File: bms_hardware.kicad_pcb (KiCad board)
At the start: 2 copper layers, 150.6 x 71.7 mm, 199 parts, among them J1 Conn_01x04_Male, J2 Conn_01x07_Female, J3 Vcc In, J4 CH_TS, J5 Conn_01x05_Male, J6 DB9_Male, Q1 2N7002, Q10 FDD86580-F085, Q11 BC848, Q12 BC848, Q13 IRF9310PbF, Q2 2N7002, Q3 2N7002, Q4 2N7002, Q5 2N7002, Q6 2N7002, Q7 DMP4051LK3, Q8 DMP4051LK3, Q9 FDD86580-F085, SW1 Reset, SW2 Select CE, SW3 SW_Push, U1 ADuM1201AR, U2 BQ76PL536APAPR, U3 BQ24618RGET, U4 TPS54331D, U5 FERD2045SB-TR, U6 STM32F407VGTx, U7 PDM1-S12-S3-S, U8 SN65HVD233, U9 INA226, Y1 8MHz

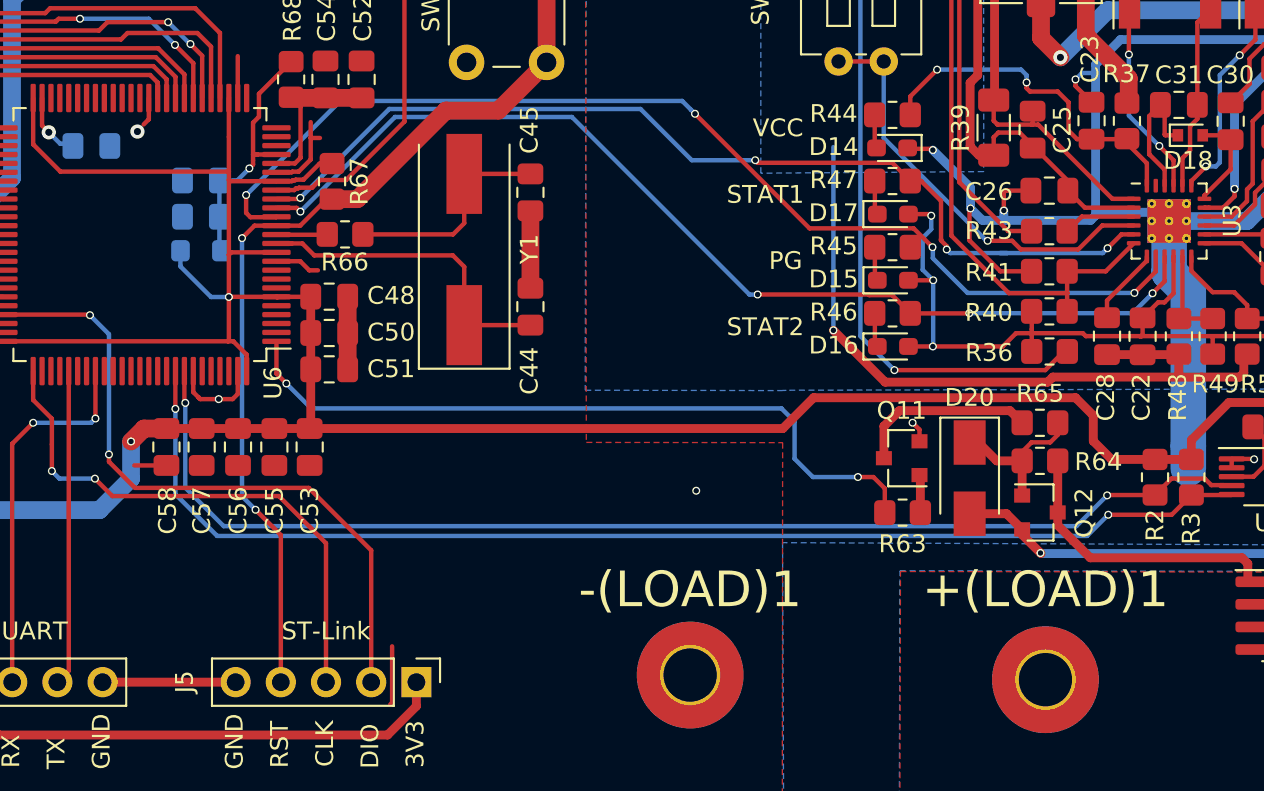
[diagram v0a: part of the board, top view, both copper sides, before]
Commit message: Adds ground plane between i2c signals
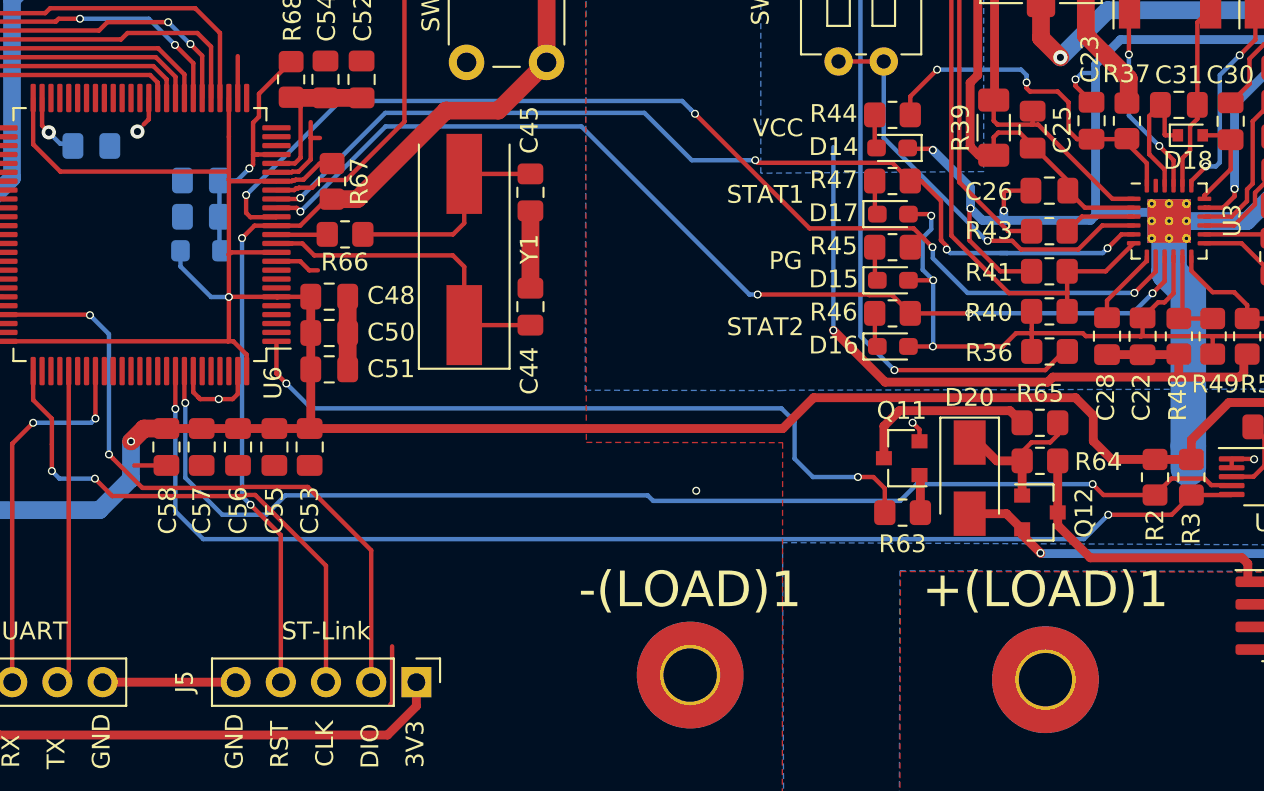
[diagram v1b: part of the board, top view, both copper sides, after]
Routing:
- net /current_sensor_ina226/SCL: track 68.2 -> 68.9 mm
- net SWCLK: track 31.0 -> 30.3 mm

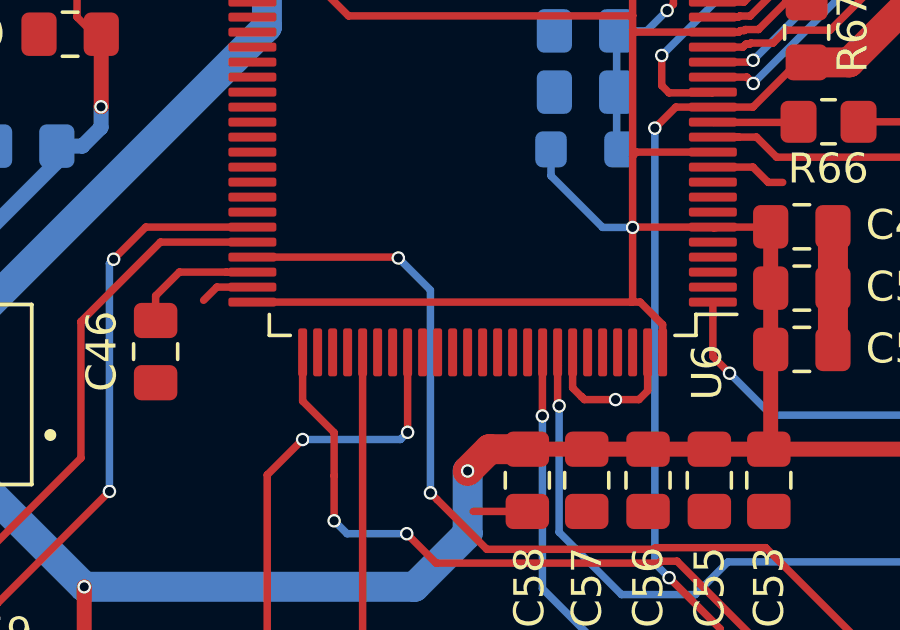
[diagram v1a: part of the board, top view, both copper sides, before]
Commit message: deletes unnecesary vias
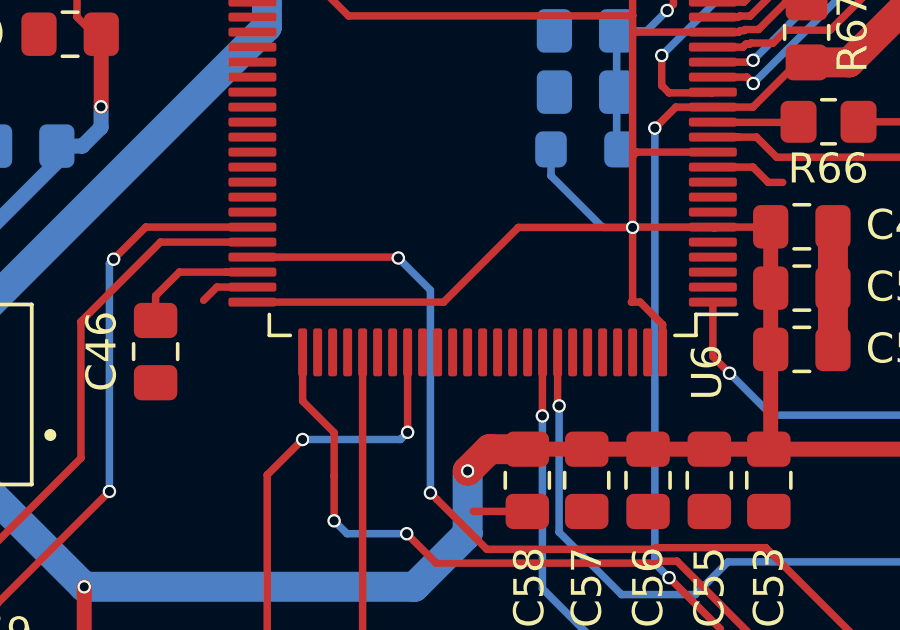
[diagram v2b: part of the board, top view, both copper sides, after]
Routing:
- net GND: track 254.4 -> 249.1 mm, vias 27 -> 26
- net VBAT: track 288.1 -> 289.2 mm

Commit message: Adds gerber files
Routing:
- net GND1: track 122.7 -> 134.0 mm
- net Net-(D13-Pad1): track 29.7 -> 19.4 mm, vias 0 -> 5
- net /bat_charger/ACP: track 46.9 -> 43.6 mm, vias 2 -> 6
- net /bat_charger/PH: vias 0 -> 5
- net /bat_charger/ACN: vias 0 -> 5
- added copper zone on B.Cu, net /bat_charger/ACN
- added copper zone on B.Cu, net /bat_charger/ACP
- added copper zone on B.Cu, net /bat_charger/PH
- added copper zone on B.Cu, net Net-(D13-Pad1)
